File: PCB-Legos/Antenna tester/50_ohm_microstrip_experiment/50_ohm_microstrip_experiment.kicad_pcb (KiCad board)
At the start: 4 copper layers, 45.7 x 66.5 mm, 10 parts, among them J1 Conn_Coaxial, J3 Conn_Coaxial, J4 Conn_Coaxial, J5 Conn_Coaxial

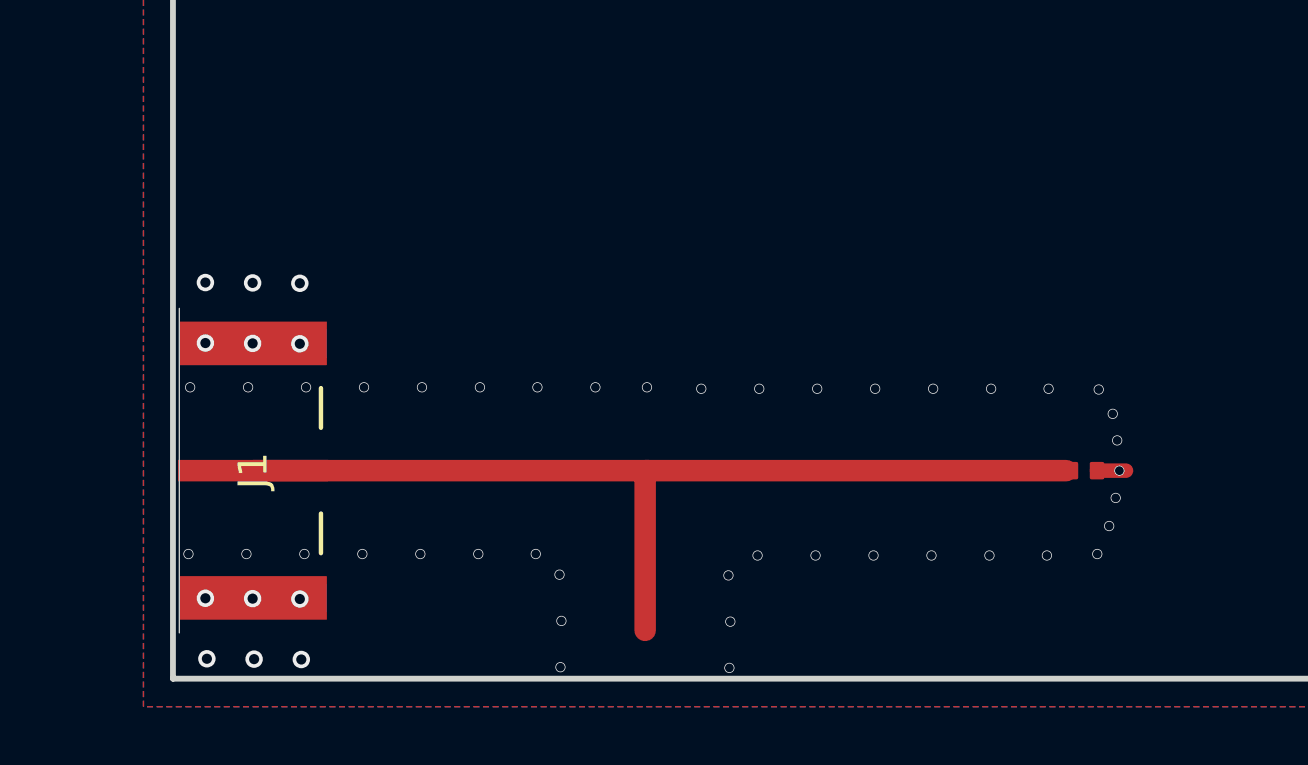
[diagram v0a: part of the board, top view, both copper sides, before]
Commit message: Moved stub to add more gnd stitching
Moved stub to add more gnd stitching
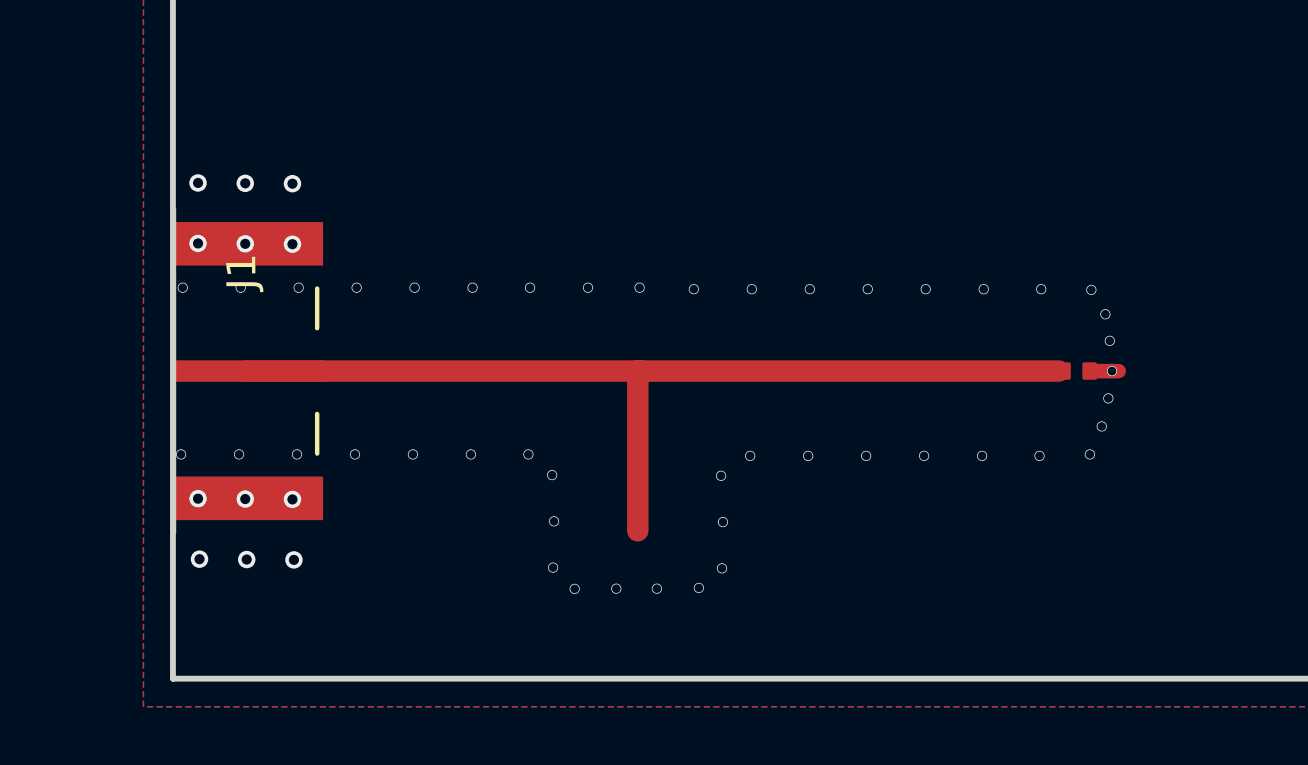
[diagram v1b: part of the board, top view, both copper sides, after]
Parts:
- moved R1 3.44 mm to (162.2, 86.2)
- moved J1 3.43 mm to (133.5, 86.2)
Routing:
- net GND: vias 198 -> 202
